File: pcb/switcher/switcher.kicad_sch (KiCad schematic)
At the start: 36 parts, among them J1 Input, J2 OUT, J3 Conn_01x02, J4 I2C, J5 I2C, SW1 toggle, SW2 reset, SW3 set, U1 SLG47115V

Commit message: Playing with text tags.
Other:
- company: (none) -> ${COMPANY}
- title: (none) -> ${TITLE}
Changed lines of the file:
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@@
 	(paper "A3")
 	(title_block
+		(title "${TITLE}")
 		(rev "${VERSION}")
+		(company "${COMPANY}")
 	)
 	(text "Switcher"

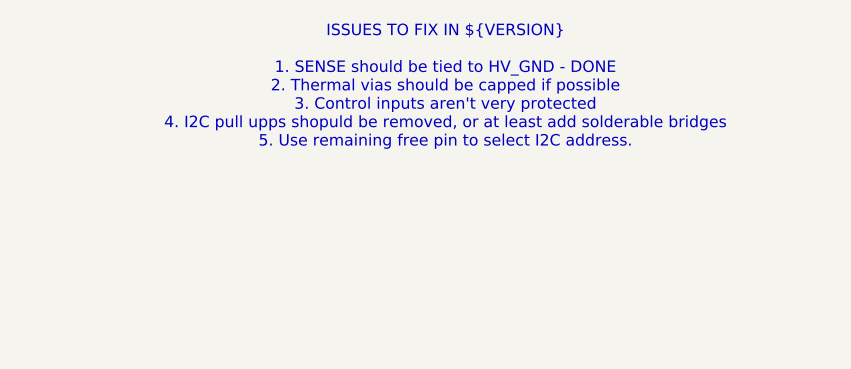
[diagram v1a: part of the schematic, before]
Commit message: Using capped vias for SLG.
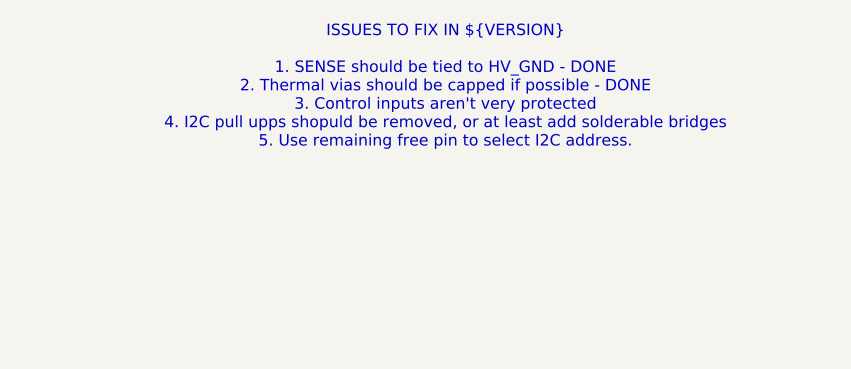
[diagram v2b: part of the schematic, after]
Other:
- note added: "ISSUES TO FIX IN ${VERSION} 1. SENSE should be tied to HV_GND - DONE 2. Thermal vias should be capped if possible - DONE 3. Control inputs aren't very protected 4. I2C pull upps shopuld be removed, or at least add solderable bridges 5. Use remaining free pin to select I2C address."
- note removed: "ISSUES TO FIX IN ${VERSION} 1. SENSE should be tied to HV_GND - DONE 2. Thermal vias should be capped if possible 3. Control inputs aren't very protected 4. I2C pull upps shopuld be removed, or at least add solderable bridges 5. Use remaining free pin to select I2C address."
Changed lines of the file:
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@@
 		)
 	)
-	(text "ISSUES TO FIX IN ${VERSION}\n\n1. SENSE should be tied to HV_GND - DONE\n2. Thermal vias should be capped if possible\n3. Control inputs aren't very protected\n4. I2C pull upps shopuld be removed, or at least add solderable bridges\n5. Use remaining free pin to select I2C address."
+	(text "ISSUES TO FIX IN ${VERSION}\n\n1. SENSE should be tied to HV_GND - DONE\n2. Thermal vias should be capped if possible - DONE\n3. Control inputs aren't very protected\n4. I2C pull upps shopuld be removed, or at least add solderable bridges\n5. Use remaining free pin to select I2C address."
 		(exclude_from_sim no)
 		(at 368.808 25.908 0)

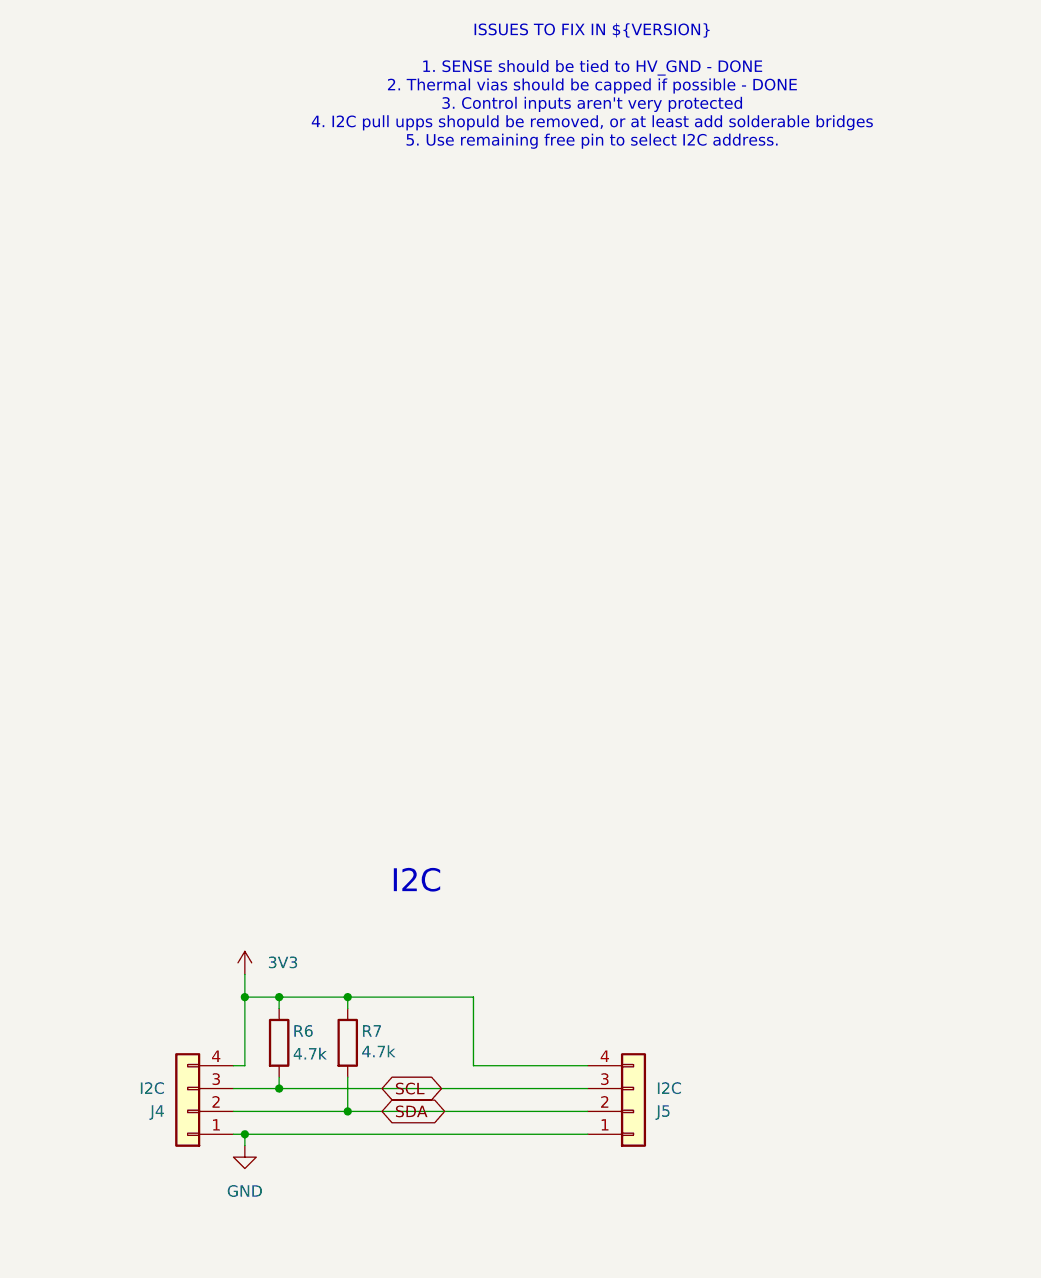
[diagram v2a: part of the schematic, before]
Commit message: Adding solderable jumbers for I2C pullups in Switcher.
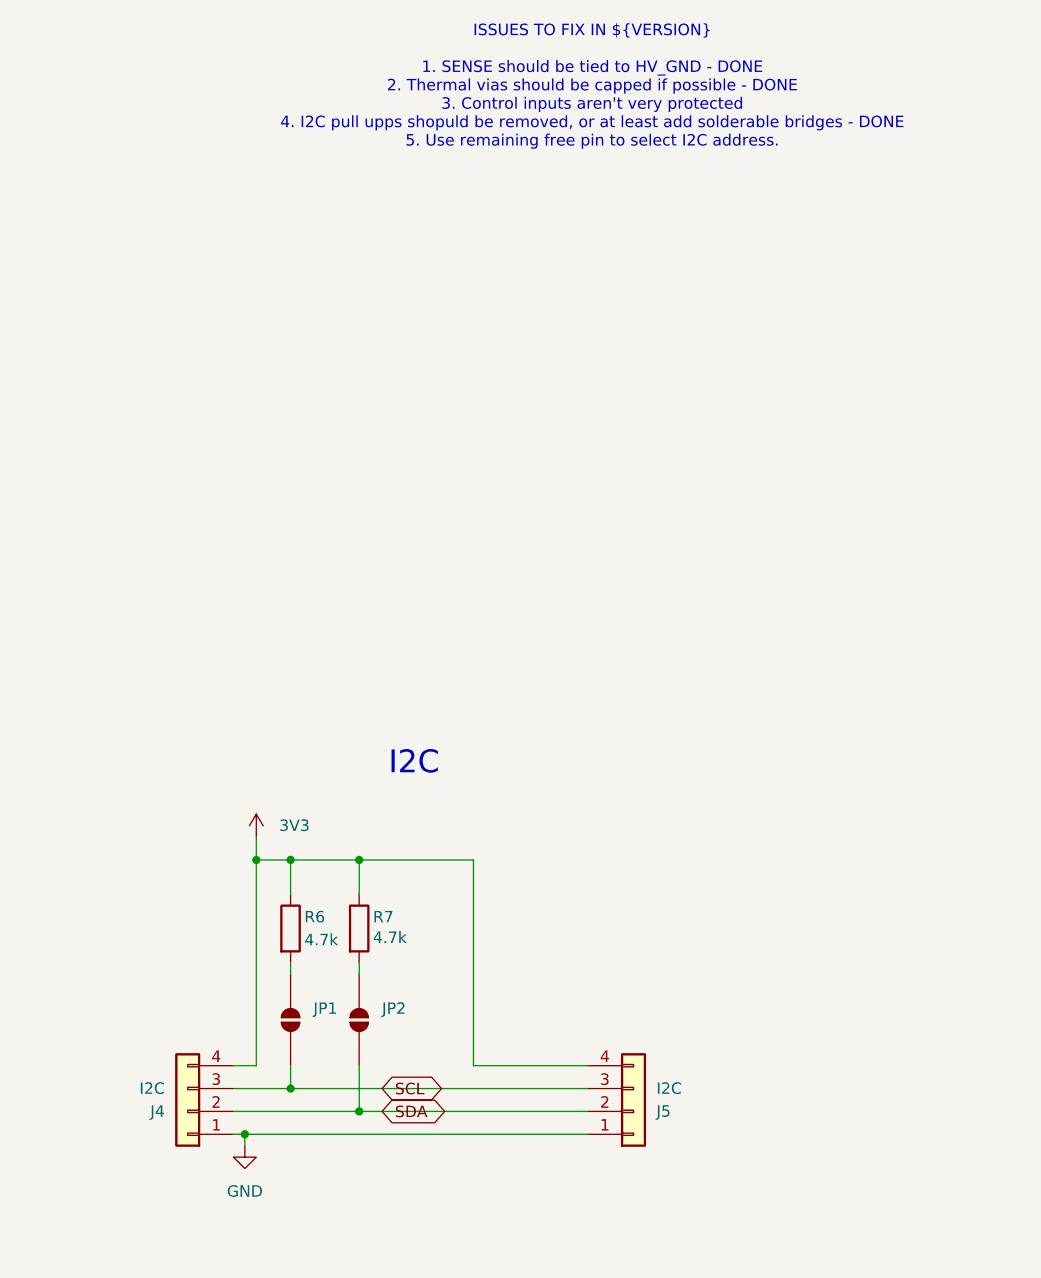
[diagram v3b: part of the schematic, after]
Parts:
- added JP1, JP2: SolderJumper_2_Open, Jumper:SolderJumper-2_P1.3mm_Open_RoundedPad1.0x1.5mm, symbol Jumper:SolderJumper_2_Open
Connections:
- net SCL: now also JP1.1 (A); no longer R6.2
- net SDA: now also JP2.1 (A); no longer R7.2
- new net: JP2.2 (B), R7.2
- new net: JP1.2 (B), R6.2
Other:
- note added: "ISSUES TO FIX IN ${VERSION} 1. SENSE should be tied to HV_GND - DONE 2. Thermal vias should be capped if possible - DONE 3. Control inputs aren't very protected 4. I2C pull upps shopuld be removed, or at least add solderable bridges - DONE 5. Use remaining free pin to select I2C address."
- note removed: "ISSUES TO FIX IN ${VERSION} 1. SENSE should be tied to HV_GND - DONE 2. Thermal vias should be capped if possible - DONE 3. Control inputs aren't very protected 4. I2C pull upps shopuld be removed, or at least add solderable bridges 5. Use remaining free pin to select I2C address."
- moved on the sheet: R6, R7

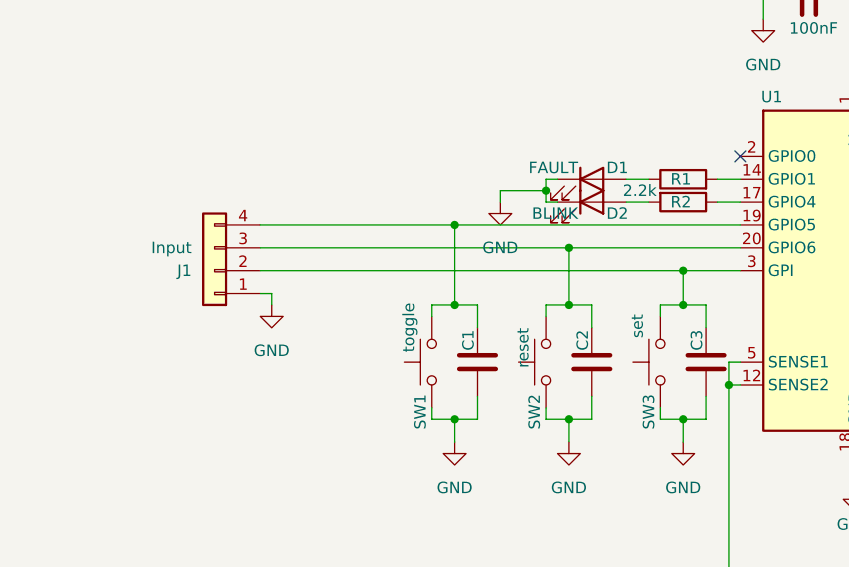
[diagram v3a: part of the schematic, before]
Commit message: Switcher: adding protection resistors.
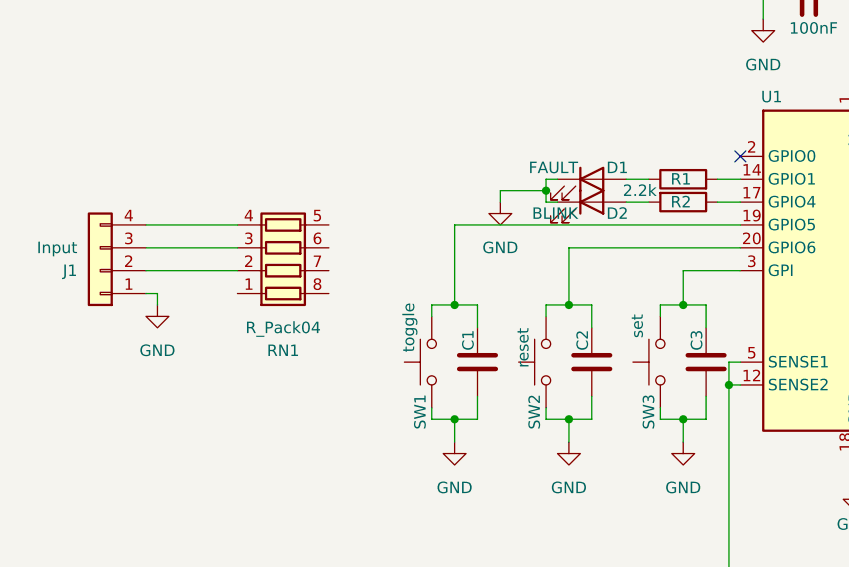
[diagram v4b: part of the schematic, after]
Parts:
- added RN1: R_Pack04, Resistor_SMD:R_Array_Concave_4x0603, symbol Device:R_Pack04
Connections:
- net at C1.2, SW1.2, U1.19 (GPIO5): no longer J1.4 (Pin_4)
- net at C3.2, SW3.2, U1.3 (GPI): no longer J1.2 (Pin_2)
- net at C2.2, SW2.2, U1.20 (GPIO6): no longer J1.3 (Pin_3)
- new net: J1.2 (Pin_2), RN1.2 (R2.1)
- new net: J1.3 (Pin_3), RN1.3 (R3.1)
- new net: J1.4 (Pin_4), RN1.4 (R4.1)
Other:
- moved on the sheet: J1
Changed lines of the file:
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@@
 	)
 	(junction
-		(at 88.9 130.81)
-		(diameter 0)
-		(color 0 0 0 0)
-	)
-	(junction
 		(at 228.6 123.19)
 		(diameter 0)
@@
 	)
 	(junction
-		(at 76.2 128.27)
-		(diameter 0)
-		(color 0 0 0 0)
-	)
-	(junction
-		(at 101.6 133.35)
-		(diameter 0)
-		(color 0 0 0 0)
-	)
-	(junction
 		(at 228.6 154.94)
 		(diameter 0)
@@
 	(wire
 		(pts
-			(xy 54.61 128.27) (xy 76.2 128.27)
-		)
-		(stroke
-			(width 0)
-			(type default)
-		)
-	)
-	(wire
-		(pts
 			(xy 342.9 134.62) (xy 342.9 139.7)
 		)
@@
 	(wire
 		(pts
-			(xy 55.88 135.89) (xy 55.88 137.16)
+			(xy 43.18 135.89) (xy 43.18 137.16)
 		)
 		(stroke
@@
 	(wire
 		(pts
+			(xy 41.91 133.35) (xy 52.07 133.35)
+		)
+		(stroke
+			(width 0)
+			(type default)
+		)
+	)
+	(wire
+		(pts
 			(xy 139.7 102.87) (xy 142.24 102.87)
 		)
@@
 	(wire
 		(pts
+			(xy 41.91 130.81) (xy 52.07 130.81)
+		)
+		(stroke
+			(width 0)
+			(type default)
+		)
+	)
+	(wire
+		(pts
 			(xy 81.28 124.46) (xy 81.28 125.73)
 		)
@@
 	(wire
 		(pts
+			(xy 41.91 128.27) (xy 52.07 128.27)
+		)
+		(stroke
+			(width 0)
+			(type default)
+		)
+	)
+	(wire
+		(pts
 			(xy 254 154.94) (xy 262.89 154.94)
 		)
@@
 	(wire
 		(pts
-			(xy 54.61 135.89) (xy 55.88 135.89)
+			(xy 41.91 135.89) (xy 43.18 135.89)
 		)
 		(stroke
@@
 	(wire
 		(pts
-			(xy 54.61 133.35) (xy 101.6 133.35)
-		)
-		(stroke
-			(width 0)
-			(type default)
-		)
-	)
-	(wire
-		(pts
-			(xy 54.61 130.81) (xy 88.9 130.81)
-		)
-		(stroke
-			(width 0)
-			(type default)
-		)
-	)
-	(wire
-		(pts
 			(xy 218.44 123.19) (xy 218.44 137.16)
 		)
@@
 	(symbol
 		(lib_id "Connector_Generic:Conn_01x04")
-		(at 49.53 133.35 180)
+		(at 36.83 133.35 180)
 		(unit 1)
 		(body_style 1)
@@
 		(dnp no)
 		(property "Reference" "J1"
-			(at 46.99 133.3501 0)
+			(at 34.29 133.3501 0)
 			(show_name no)
 			(do_not_autoplace no)
@@
 		)
 		(property "Value" "Input"
-			(at 46.99 130.8101 0)
+			(at 34.29 130.8101 0)
 			(show_name no)
 			(do_not_autoplace no)
@@
 		)
 		(property "Footprint" "Connector_Phoenix_MC:PhoenixContact_MCV_1,5_4-G-3.5_1x04_P3.50mm_Vertical"
-			(at 49.53 133.35 0)
+			(at 36.83 133.35 0)
 			(hide yes)
 			(show_name no)
@@
 		)
 		(property "Datasheet" ""
-			(at 49.53 133.35 0)
+			(at 36.83 133.35 0)
 			(hide yes)
 			(show_name no)
@@
 		)
 		(property "Description" "Generic connector, single row, 01x04, script generated (kicad-library-utils/schlib/autogen/connector/)"
-			(at 49.53 133.35 0)
+			(at 36.83 133.35 0)
 			(hide yes)
 			(show_name no)
@@
 	(symbol
 		(lib_id "power:GND")
-		(at 55.88 137.16 0)
+		(at 43.18 137.16 0)
 		(unit 1)
 		(body_style 1)
@@
 		(fields_autoplaced yes)
 		(property "Reference" "#PWR01"
-			(at 55.88 143.51 0)
+			(at 43.18 143.51 0)
 			(hide yes)
 			(show_name no)
@@
 		)
 		(property "Value" "GND"
-			(at 55.88 142.24 0)
+			(at 43.18 142.24 0)
 			(show_name no)
 			(do_not_autoplace no)
@@
 		)
 		(property "Footprint" ""
-			(at 55.88 137.16 0)
+			(at 43.18 137.16 0)
 			(hide yes)
 			(show_name no)
@@
 		)
 		(property "Datasheet" ""
-			(at 55.88 137.16 0)
+			(at 43.18 137.16 0)
 			(hide yes)
 			(show_name no)
@@
 		)
 		(property "Description" "Power symbol creates a global label with name \"GND\" , ground"
-			(at 55.88 137.16 0)
+			(at 43.18 137.16 0)
 			(hide yes)
 			(show_name no)
@@
 					(unit 1)
 				)
+			)
+		)
+	)
+	(symbol
+		(lib_id "Device:R_Pack04")
+		(at 57.15 130.81 270)
+		(mirror x)
+		(unit 1)
+		(body_style 1)
+		(exclude_from_sim no)
+		(in_bom yes)
+		(on_board yes)
+		(in_pos_files yes)
+		(dnp no)
+		(property "Reference" "RN1"
+			(at 57.15 142.24 90)
+			(show_name no)
+			(do_not_autoplace no)
+			(effects
+				(font
+					(size 1.27 1.27)
+				)
+			)
+		)
+		(property "Value" "R_Pack04"
+			(at 57.15 139.7 90)
+			(show_name no)
+			(do_not_autoplace no)
+			(effects
+				(font
+					(size 1.27 1.27)
+				)
+			)
+		)
+		(property "Footprint" "Resistor_SMD:R_Array_Concave_4x0603"
+			(at 57.15 123.825 90)
+			(hide yes)
+			(show_name no)
+			(do_not_autoplace no)
+			(effects
+				(font
+					(size 1.27 1.27)
+				)
+			)
+		)
+		(property "Datasheet" ""
+			(at 57.15 130.81 0)
+			(hide yes)
+			(show_name no)
+			(do_not_autoplace no)
+			(effects
+				(font
+					(size 1.27 1.27)
+				)
+			)
+		)
+		(property "Description" "4 resistor network, parallel topology"
+			(at 57.15 130.81 0)
+			(hide yes)
+			(show_name no)
+			(do_not_autoplace no)
+			(effects
+				(font
+					(size 1.27 1.27)
+				)
+			)
+		)
+		(pin "2"
+		)
+		(pin "4"
+		)
+		(pin "5"
+		)
+		(pin "3"
+		)
+		(pin "1"
+		)
+		(pin "6"
+		)
+		(pin "8"
+		)
+		(pin "7"
+		)
+		(instances
+			(project "switcher"
+				(path "/2155cca2-5ec1-4d94-9553-ebcda519e5b5"
+					(reference "RN1")
+					(unit 1)
+				)

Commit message: Switcher: fixing ERC/DRC issues.
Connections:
- net at C1.2, SW1.2, U1.19 (GPIO5): now also RN1.5 (R4.2)
- net at C3.2, SW3.2, U1.3 (GPI): now also RN1.7 (R2.2)
- net at C2.2, SW2.2, U1.20 (GPIO6): now also RN1.6 (R3.2)
- no-connect marks 1 -> 3
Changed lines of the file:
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@@
+	)
+	(junction
+		(at 101.6 133.35)
+		(diameter 0)
+		(color 0 0 0 0)
 	)
 	(junction
@@
 	)
 	(junction
+		(at 88.9 130.81)
+		(diameter 0)
+		(color 0 0 0 0)
+	)
+	(junction
 		(at 342.9 139.7)
 		(diameter 0)
@@
 	)
 	(junction
+		(at 76.2 128.27)
+		(diameter 0)
+		(color 0 0 0 0)
+	)
+	(junction
 		(at 254 154.94)
 		(diameter 0)
@@
 		(diameter 0)
 		(color 0 0 0 0)
+	)
+	(no_connect
+		(at 62.23 135.89)
 	)
 	(no_connect
 		(at 107.95 120.65)
 	)
+	(no_connect
+		(at 52.07 135.89)
+	)
 	(wire
 		(pts
@@
 	(wire
 		(pts
+			(xy 62.23 128.27) (xy 76.2 128.27)
+		)
+		(stroke
+			(width 0)
+			(type default)
+		)
+	)
+	(wire
+		(pts
 			(xy 342.9 134.62) (xy 342.9 139.7)
 		)
@@
 	(wire
 		(pts
+			(xy 62.23 133.35) (xy 101.6 133.35)
+		)
+		(stroke
+			(width 0)
+			(type default)
+		)
+	)
+	(wire
+		(pts
 			(xy 139.7 102.87) (xy 142.24 102.87)
 		)
@@
 		)
 		(stroke
+			(width 0)
+			(type default)
+		)
+	)
+	(wire
+		(pts
+			(xy 62.23 130.81) (xy 88.9 130.81)
+		)
+		(stroke

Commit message: Switcher: Using PIN3 on SLG to select I2C bit3.
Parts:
- added Bit3: SolderJumper_2_Open, Jumper:SolderJumper-2_P1.3mm_Open_RoundedPad1.0x1.5mm, symbol Jumper:SolderJumper_2_Open
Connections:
- net GND: now also Bit3.1 (A)
- net at C3.2, RN1.7 (R2.2), SW3.2: now also U1.2 (GPIO0); no longer U1.3 (GPI)
- new net: Bit3.2 (B), U1.3 (GPI)
- no-connect marks 3 -> 2
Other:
- note removed: "ISSUES TO FIX IN ${VERSION} 1. SENSE should be tied to HV_GND - DONE 2. Thermal vias should be capped if possible - DONE 3. Control inputs aren't very protected 4. I2C pull upps shopuld be removed, or at least add solderable bridges - DONE 5. Use remaining free pin to select I2C address."
- moved on the sheet: C1, C2, C3, C4, C5, D1, D2, D3, J1, J2, R1, R2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

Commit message: Switcher: Adding TVS diodes.
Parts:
- added U2: TPD4E02B04DQA, Package_SON:USON-10_2.5x1.0mm_P0.5mm, symbol Power_Protection:TPD4E02B04DQA
- RN1: value R_Pack04 -> 100
- renumbered JP1 to PU1, JP2 to PU2
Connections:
- net GND: now also U2.3 (G), U2.8 (G)
- net at J1.2 (Pin_2), RN1.2 (R2.1): now also U2.4 (IO3)
- net at J1.3 (Pin_3), RN1.3 (R3.1): now also U2.2 (IO2)
- net at J1.4 (Pin_4), RN1.4 (R4.1): now also U2.1 (IO1)
- no-connect marks 2 -> 3
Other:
- moved on the sheet: C6, D4, D5, J3, R4, R5
